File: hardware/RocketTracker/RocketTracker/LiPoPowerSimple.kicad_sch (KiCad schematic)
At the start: 32 parts, among them J201 LiPo, SW201 Power Switch, U201 MCP73871-1CC, U202 TPS63070RNMR

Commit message: シルク入れた
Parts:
- added LED202: CHARGE, LED_SMD:LED_0805_2012Metric, symbol Device:LED
- added R205: 10k, Resistor_SMD:R_0402_1005Metric, symbol Device:R
- added R208: 1k, Resistor_SMD:R_0402_1005Metric, symbol Device:R
- LED203: renamed from LED202; value CHARGE -> FULL
- renumbered LED203 to LED204, R204 to R203, R203 to R204, R205 to R206, R206 to R207, R208 to R209, R207 to R210, R209 to R211, R210 to R212, R211 to R213, R212 to R214
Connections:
- net GND: now also R205.1; no longer R203.1
- net VDD: now also R208.2
- net at U201.8 (STAT1/~{LBO}): now also LED202.1 (K); no longer LED203.1 (K)
- net VPP: now reaches C204.1, F202.1, U201.14 (V_{BAT}), U201.15 (V_{BAT}), U201.16 (V_{BAT_SENSE})
- net at R203.1, U201.5 (THERM): now also R205.2; no longer R203.2
- new net: LED202.2 (A), R208.1

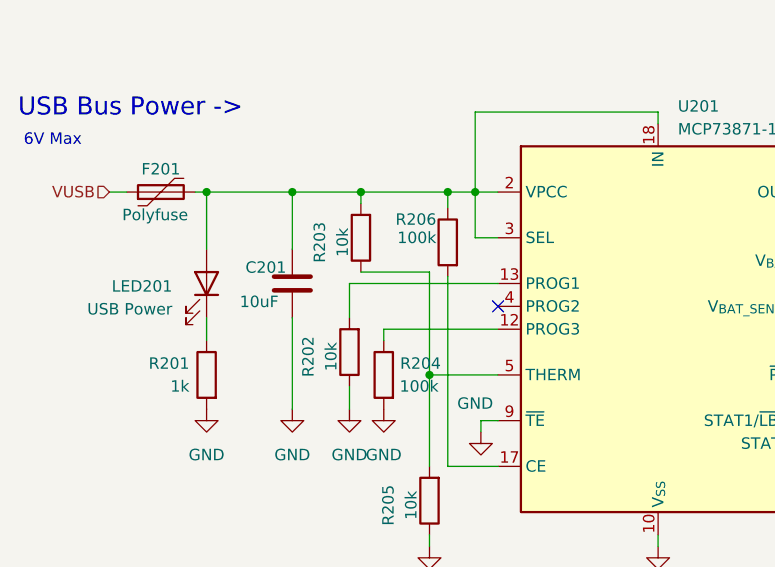
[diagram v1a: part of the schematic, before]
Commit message: 充電ICのTHERMピンへの入力変更
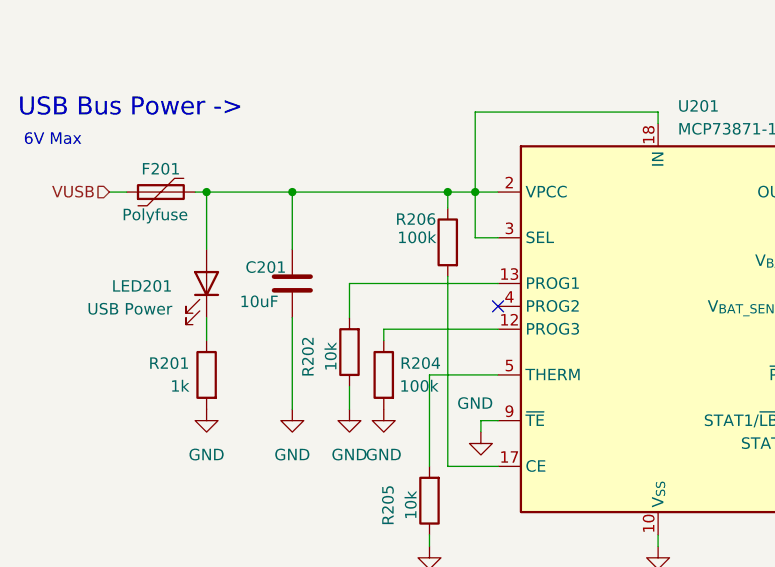
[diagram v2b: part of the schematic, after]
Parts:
- removed R203: 10k, Resistor_SMD:R_0402_1005Metric, symbol Device:R
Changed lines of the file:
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@@
 	)
 	(junction
-		(at 68.58 116.84)
-		(diameter 0)
-		(color 0 0 0 0)
-	)
-	(junction
 		(at 229.235 60.96)
 		(diameter 0)
@@
 	)
 	(junction
-		(at 60.96 96.52)
-		(diameter 0)
-		(color 0 0 0 0)
-	)
-	(junction
 		(at 186.69 104.14)
 		(diameter 0)
@@
 	(wire
 		(pts
-			(xy 53.34 96.52) (xy 60.96 96.52)
+			(xy 53.34 96.52) (xy 70.612 96.52)
 		)
 		(stroke
@@
 	(wire
 		(pts
-			(xy 60.96 105.41) (xy 68.58 105.41)
-		)
-		(stroke
-			(width 0)
-			(type default)
-		)
-	)
-	(wire
-		(pts
 			(xy 116.332 52.07) (xy 121.285 52.07)
 		)
@@
 	(wire
 		(pts
-			(xy 68.58 105.41) (xy 68.58 116.84)
-		)
-		(stroke
-			(width 0)
-			(type default)
-		)
-	)
-	(wire
-		(pts
 			(xy 168.275 58.42) (xy 163.83 58.42)
 		)
@@
 	(wire
 		(pts
-			(xy 60.96 96.52) (xy 70.612 96.52)
-		)
-		(stroke
-			(width 0)
-			(type default)
-		)
-	)
-	(wire
-		(pts
 			(xy 212.725 64.77) (xy 212.725 52.07)
 		)
@@
 	(wire
 		(pts
-			(xy 60.96 96.52) (xy 60.96 97.79)
-		)
-		(stroke
-			(width 0)
-			(type default)
-		)
-	)
-	(wire
-		(pts
 			(xy 93.98 87.63) (xy 73.66 87.63)
 		)
@@
 					(unit 1)
 				)
-			)
-		)
-	)
-	(symbol
-		(lib_id "Device:R")
-		(at 60.96 101.6 180)
-		(unit 1)
-		(exclude_from_sim no)
-		(in_bom yes)
-		(on_board yes)
-		(dnp no)
-		(property "Reference" "R203"
-			(at 56.388 102.108 90)
-			(effects
-				(font
-					(size 1.27 1.27)
-				)
-			)
-		)
-		(property "Value" "10k"
-			(at 58.928 102.108 90)
-			(effects
-				(font
-					(size 1.27 1.27)
-				)
-			)
-		)
-		(property "Footprint" "Resistor_SMD:R_0402_1005Metric"
-			(at 62.738 101.6 90)
-			(effects
-				(font
-					(size 1.27 1.27)
-				)
-				(hide yes)
-			)
-		)
-		(property "Datasheet" "~"
-			(at 60.96 101.6 0)
-			(effects
-				(font
-					(size 1.27 1.27)
-				)
-				(hide yes)
-			)
-		)
-		(property "Description" "Resistor"
-			(at 60.96 101.6 0)
-			(effects
-				(font
-					(size 1.27 1.27)
-				)
-				(hide yes)
-			)
-		)
-		(property "LCSC" "C25744"
-			(at 60.96 101.6 0)
-			(effects
-				(font
-					(size 1.27 1.27)
-				)
-				(hide yes)
-			)
-		)
-		(pin "1"
-		)
-		(pin "2"
-		)
-		(instances
-			(project "RocketTracker"
-				(path "/cba598e6-eeb3-4d1f-bd55-65e7525b0953/12adc2e5-90e7-4861-a57f-1b2510c964d9"
-					(reference "R203")
-					(unit 1)
-				)

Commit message: コンデンサ，ダイオード追加
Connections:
- net MCPOUT: now reaches C202.1, C203.1, C205.1, R207.1, U201.1 (OUT), U201.20 (OUT), U202.12_13 (VIN)
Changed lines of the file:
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@@
+	)
+	(junction
+		(at 111.76 52.07)
+		(diameter 0)
+		(color 0 0 0 0)
 	)
 	(junction
@@
 		(pts
 			(xy 204.47 52.07) (xy 212.725 52.07)
+		)
+		(stroke
+			(width 0)
+			(type default)
+		)
+	)
+	(wire
+		(pts
+			(xy 107.95 52.07) (xy 111.76 52.07)
 		)
 		(stroke
@@
 		(effects
 			(font
+				(size 1.27 1.27)
+			)
+			(justify right)
+		)
+	)
+	(hierarchical_label "MCPOUT"
+		(shape input)
+		(at 107.95 52.07 180)
+		(effects
+			(font
